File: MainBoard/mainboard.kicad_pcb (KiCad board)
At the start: 2 copper layers, 40 x 36 mm, 47 parts, among them J2 Matrix_in, J3 Conn_01x02_Pin, P1 USB_C_Receptacle_USB2.0_14P, Q1 AO3400A, Q2 AO3401A, Q3 PT1921C, Q4 PT1921C, SW1 ENABLE, SW2 BOOT, U1 MCP73811T-420I-OT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

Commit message: Add logo and update project variables
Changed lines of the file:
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@@
 	)
 	(paper "A4")
+	(title_block
+		(title "${ProjectTitle}")
+		(date "2025-11-23")
+		(rev "${Revision}")
+		(company "${Company}")
+	)
 	(layers
 		(0 "F.Cu" signal)
@@
 		)
 	)
+	(gr_poly
+		(pts
+			(xy 241.880008 87.97179) (xy 242.205304 88.219015) (xy 241.880008 88.453228) (xy 241.89302 89.192805)
+			(xy 242.192292 89.505088) (xy 243.428414 89.518101) (xy 243.415402 89.140757) (xy 243.121385 88.875785)
+			(xy 243.410802 88.636973) (xy 243.40778 87.953007) (xy 243.090107 87.618375) (xy 241.880008 87.618374)
+		)
+		(stroke
+			(width 0)
+			(type solid)
+		)
+		(fill yes)
+		(layer "B.SilkS")
+	)
+	(gr_poly
+		(pts
+			(xy 239.646024 87.643934) (xy 239.203623 88.01989) (xy 239.203623 87.663453) (xy 238.800256 87.65044)
+			(xy 238.754715 89.390674) (xy 239.171093 89.403687) (xy 239.621906 89.070443) (xy 239.626506 89.403687)
+			(xy 240.003849 89.429709) (xy 240.010356 87.630924)
+		)
+		(stroke
+			(width 0)
+			(type solid)
+		)
+		(fill yes)
+		(layer "B.SilkS")
+	)
+	(gr_poly
+		(pts
+			(xy 241.882124 85.50053) (xy 241.928128 86.788634) (xy 242.507775 87.175065) (xy 243.483053 87.165865)
+			(xy 243.44625 85.00369) (xy 242.286957 84.985288)
+		)
+		(stroke
+			(width 0)
+			(type solid)
+		)
+		(fill yes)
+		(layer "B.SilkS")
+	)
+	(gr_poly
+		(pts
+			(xy 238.662901 85.11791) (xy 238.331674 85.403133) (xy 238.350076 86.093188) (xy 238.874518 86.544025)
+			(xy 238.40528 87.215679) (xy 239.693384 87.215679) (xy 239.683033 86.147243) (xy 239.673976 85.40299)
+			(xy 239.665782 85.044305)
+		)
+		(stroke
+			(width 0)
+			(type solid)
+		)
+		(fill yes)
+		(layer "B.SilkS")
+	)
+	(gr_poly
+		(pts
+			(xy 240.296822 85.081109) (xy 240.057602 85.449137) (xy 240.085204 86.948858) (xy 240.361227 87.215679)
+			(xy 241.308904 87.215679) (xy 241.612528 86.829249) (xy 241.557324 85.412334) (xy 241.170892 84.979899)
+		)
+		(stroke
+			(width 0)
+			(type solid)
+		)
+		(fill yes)
+		(layer "B.SilkS")
+	)
+	(gr_poly
+		(pts
+			(xy 236.078147 85.61252) (xy 236.363369 85.870141) (xy 236.073546 86.178365) (xy 236.078146 86.882223)
+			(xy 236.38177 87.195048) (xy 237.320246 87.204247) (xy 237.311045 86.845418) (xy 237.044224 86.569396)
+			(xy 237.324846 86.316375) (xy 237.301844 85.437705) (xy 237.025823 85.152483) (xy 236.54735 85.14488)
+			(xy 236.302095 85.140172) (xy 236.068946 85.134083)
+		)
+		(stroke
+			(width 0)
+			(type solid)
+		)
+		(fill yes)
+		(layer "B.SilkS")
+	)
+	(gr_poly
+		(pts
+			(xy 236.131492 89.421897) (xy 236.391729 89.421897) (xy 236.704012 88.966485) (xy 236.925214 89.369851)
+			(xy 237.276533 89.408886) (xy 237.234341 87.714576) (xy 236.961092 87.714574) (xy 236.66182 88.156977)
+			(xy 236.414596 87.675539) (xy 236.0893 87.649515)
+		)
+		(stroke
+			(width 0)
+			(type solid)
+		)
+		(fill yes)
+		(layer "B.SilkS")
+	)
+	(gr_poly
+		(pts
+			(xy 237.441197 87.700912) (xy 237.438177 88.037641) (xy 237.831554 88.308272) (xy 237.870589 89.368273)
+			(xy 238.251089 89.388907) (xy 238.229666 88.312083) (xy 238.550688 88.063662) (xy 238.550688 87.699331)
+		)
+		(stroke
+			(width 0)
+			(type solid)
+		)
+		(fill yes)
+		(layer "B.SilkS")
+	)
+	(gr_poly
+		(pts
+			(xy 237.664552 86.155361) (xy 237.682666 86.871582) (xy 237.6914 87.113137) (xy 237.699055 87.213447)
+			(xy 237.701598 87.216658) (xy 237.705704 87.219408) (xy 237.711266 87.221721) (xy 237.718175 87.223618)
+			(xy 237.735606 87.226264) (xy 237.757135 87.227536) (xy 237.781898 87.227621) (xy 237.809033 87.22671)
+			(xy 237.866969 87.222648) (xy 237.924042 87.216862) (xy 237.973352 87.21086) (xy 238.021081 87.204247)
+			(xy 237.956676 85.13408) (xy 237.643851 85.124877)
+		)
+		(stroke
+			(width 0)
+			(type solid)
+		)
+		(fill yes)
+		(layer "B.SilkS")
+	)
+	(gr_poly
+		(pts
+			(xy 240.306853 87.620934) (xy 240.319865 89.013198) (xy 240.714819 89.423533) (xy 241.576813 89.431483)
+			(xy 241.550789 89.067152) (xy 241.251518 88.819927) (xy 241.55999 88.53157) (xy 241.566169 87.614428)
+		)
+		(stroke
+			(width 0)
+			(type solid)
+		)
+		(fill yes)
+		(layer "B.SilkS")
+	)
 	(gr_arc
 		(start 210 57.5)
@@
 		)
 	)
+	(gr_text "${ProjectTitle}\n${BoardName}\n${Revision}\n${CURRENT_DATE}"
+		(at 249.301 80.772 0)
+		(layer "B.SilkS")
+		(effects
+			(font
+				(size 0.8 0.8)
+				(thickness 0.1)
+			)
+			(justify left bottom mirror)
+		)
+	)
 	(segment
 		(start 233.2 83.157)
@@
 		)
 	)
+	(group ""
+		(members "266e6944-0079-4666-83a3-e5b7941ad04f" "4c13fc4f-029e-453c-af08-dab2ec1ae9e3"
+			"57f32ce7-ba73-4aea-9604-62c5af794000" "75a914f0-7c5a-49d6-9309-c0318d4afe13"
+			"78e57f72-71b5-478a-924d-91bb9fb35bc8" "81bec8fe-bd86-49cc-95ca-1a8c1b3069a6"
+			"b7759a50-2b5b-4682-b69a-35a2a0acd21f" "d22c1078-6e4b-4e05-84c6-aab0799b44cc"
+			"efca9253-d740-4025-85f1-329ca3a23da6" "f762c3f1-2f70-4ef2-aa70-9d0ad88f10d7"
+		)
+	)

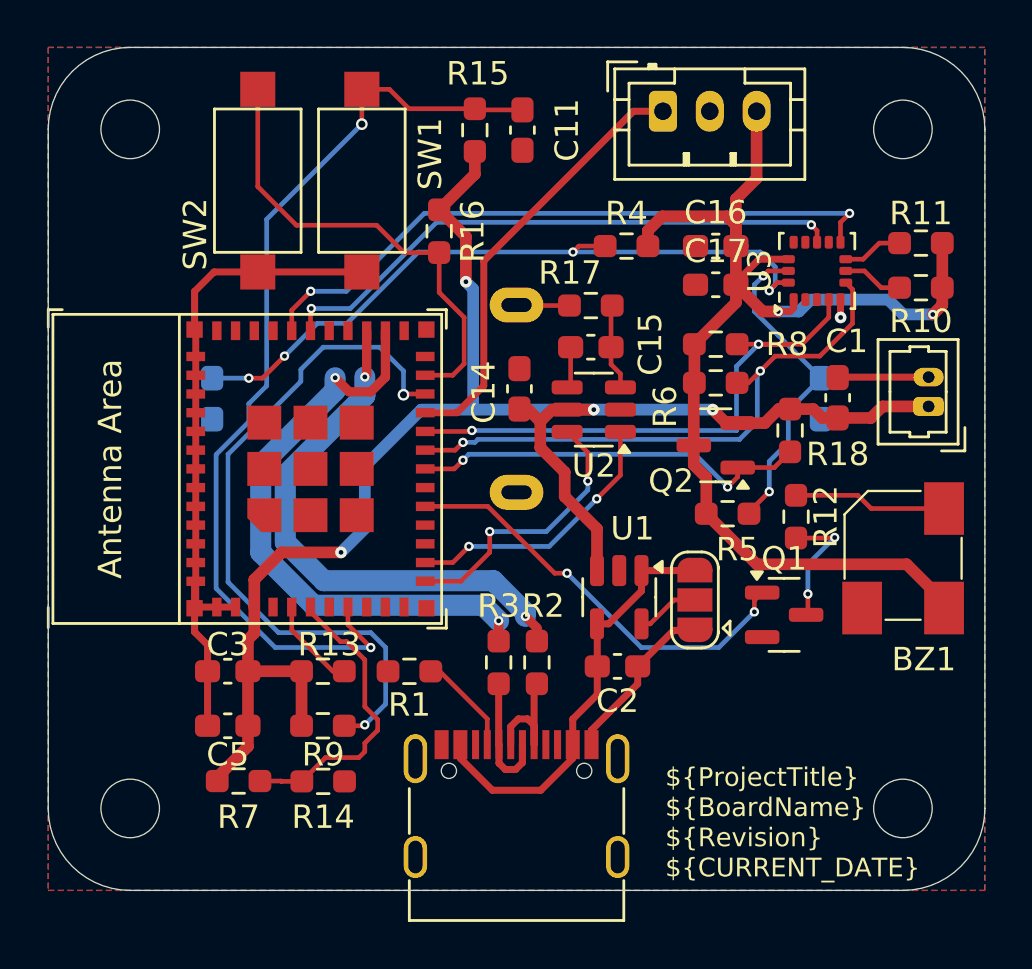
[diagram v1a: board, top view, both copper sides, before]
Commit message: clean project, change location of some libraries
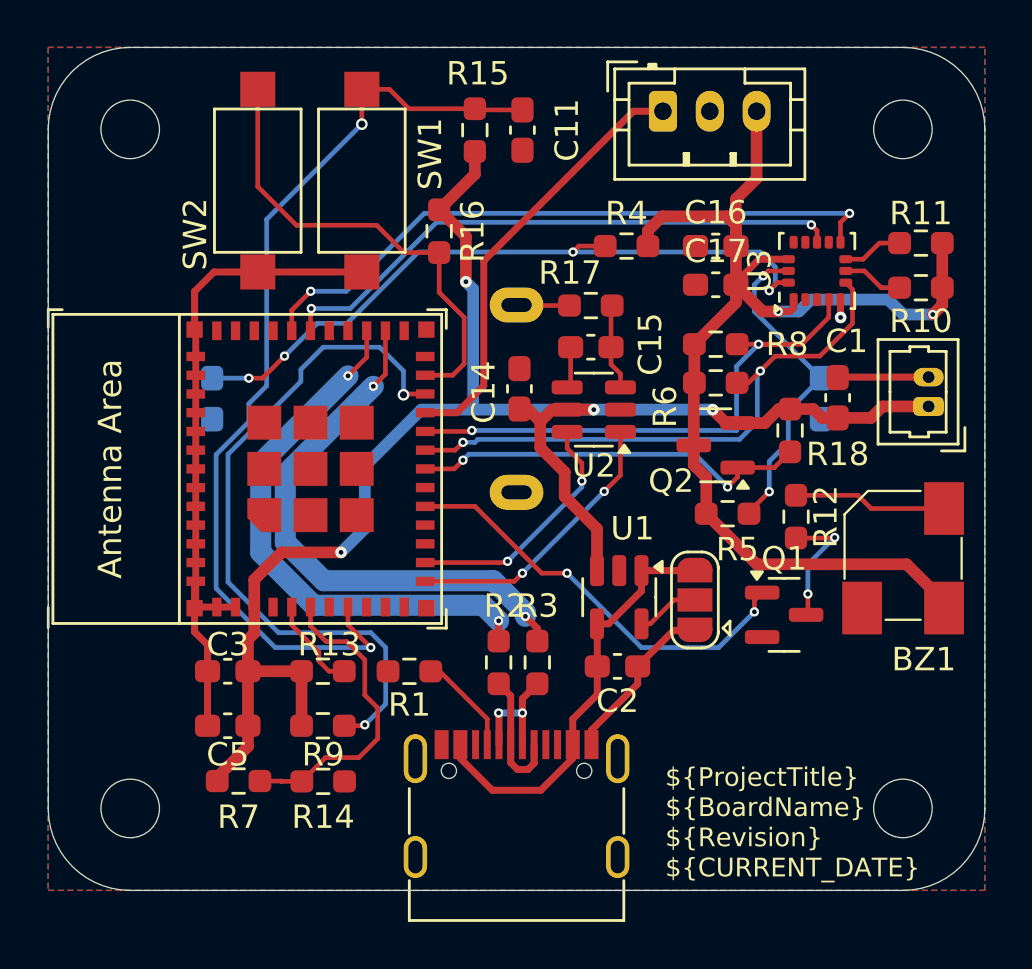
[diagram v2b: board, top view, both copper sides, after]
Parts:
- moved R3 1.65 mm to (230.9, 80.3)
- moved R2 1.63 mm to (229.2, 80.3)
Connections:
- U5 pad 12: /CPU/SYNC -> /CPU/TOUCH
- U5 pad 13: /CPU/TOUCH -> /CPU/SYNC
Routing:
- net /CPU/_USB-: track 25.6 -> 23.7 mm
- net /CPU/SYNC: track 11.9 -> 10.6 mm
- net /CPU/USB-: track 5.40 -> 5.66 mm, vias 0 -> 2

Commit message: Change some opto signals
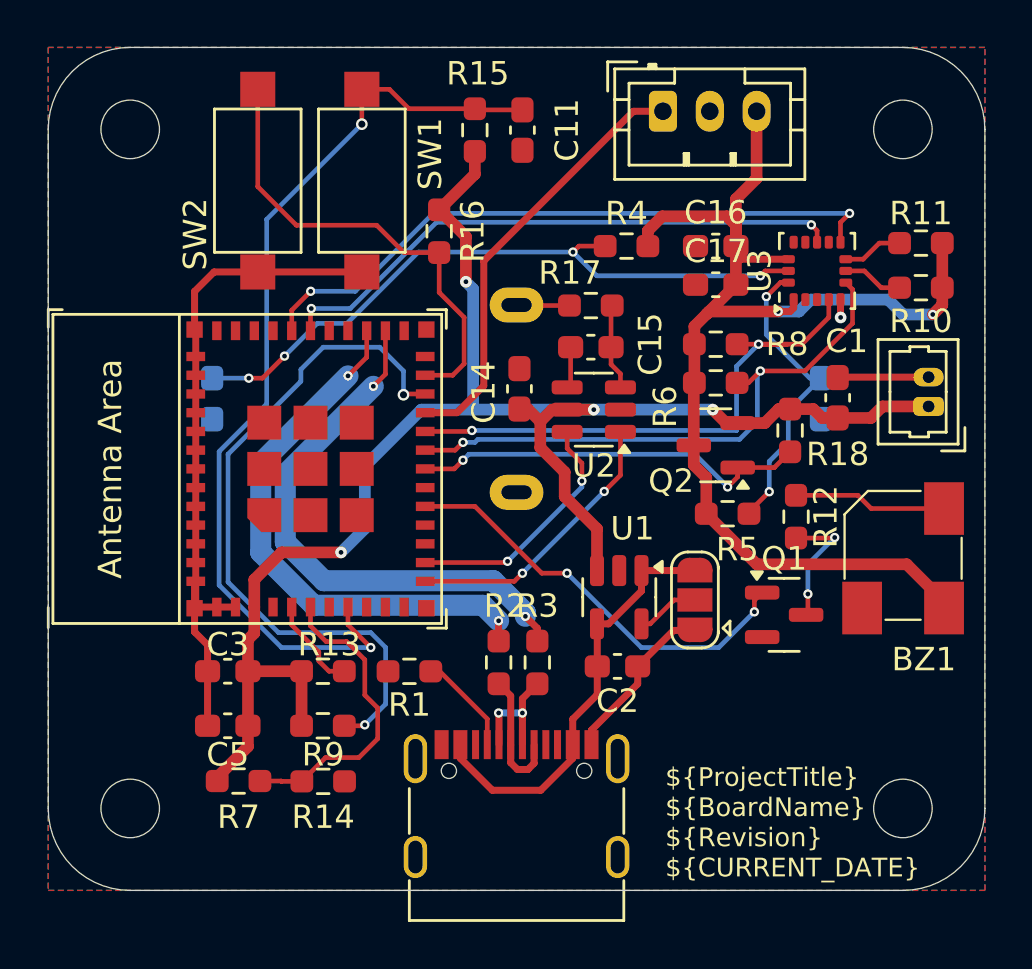
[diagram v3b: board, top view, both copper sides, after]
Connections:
- U3 pad 15: /utils/OPTO2 -> /utils/OPTO1
- U3 pad 16: /utils/OPTO1 -> /utils/OPTO2
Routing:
- net /utils/OPTO1: track 30.1 -> 28.8 mm
- net /utils/OPTO2: track 13.9 -> 13.0 mm
- net VPP: track 53.0 -> 53.9 mm
